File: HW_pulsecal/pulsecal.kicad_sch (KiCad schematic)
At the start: 39 parts, among them J1 BNC_CONN, J4 Conn_01x04, Q3 FDG6301N, U1 TLV9061IDBVR, U2 TLV9061IDBVR, U5 STM32G030C8Tx

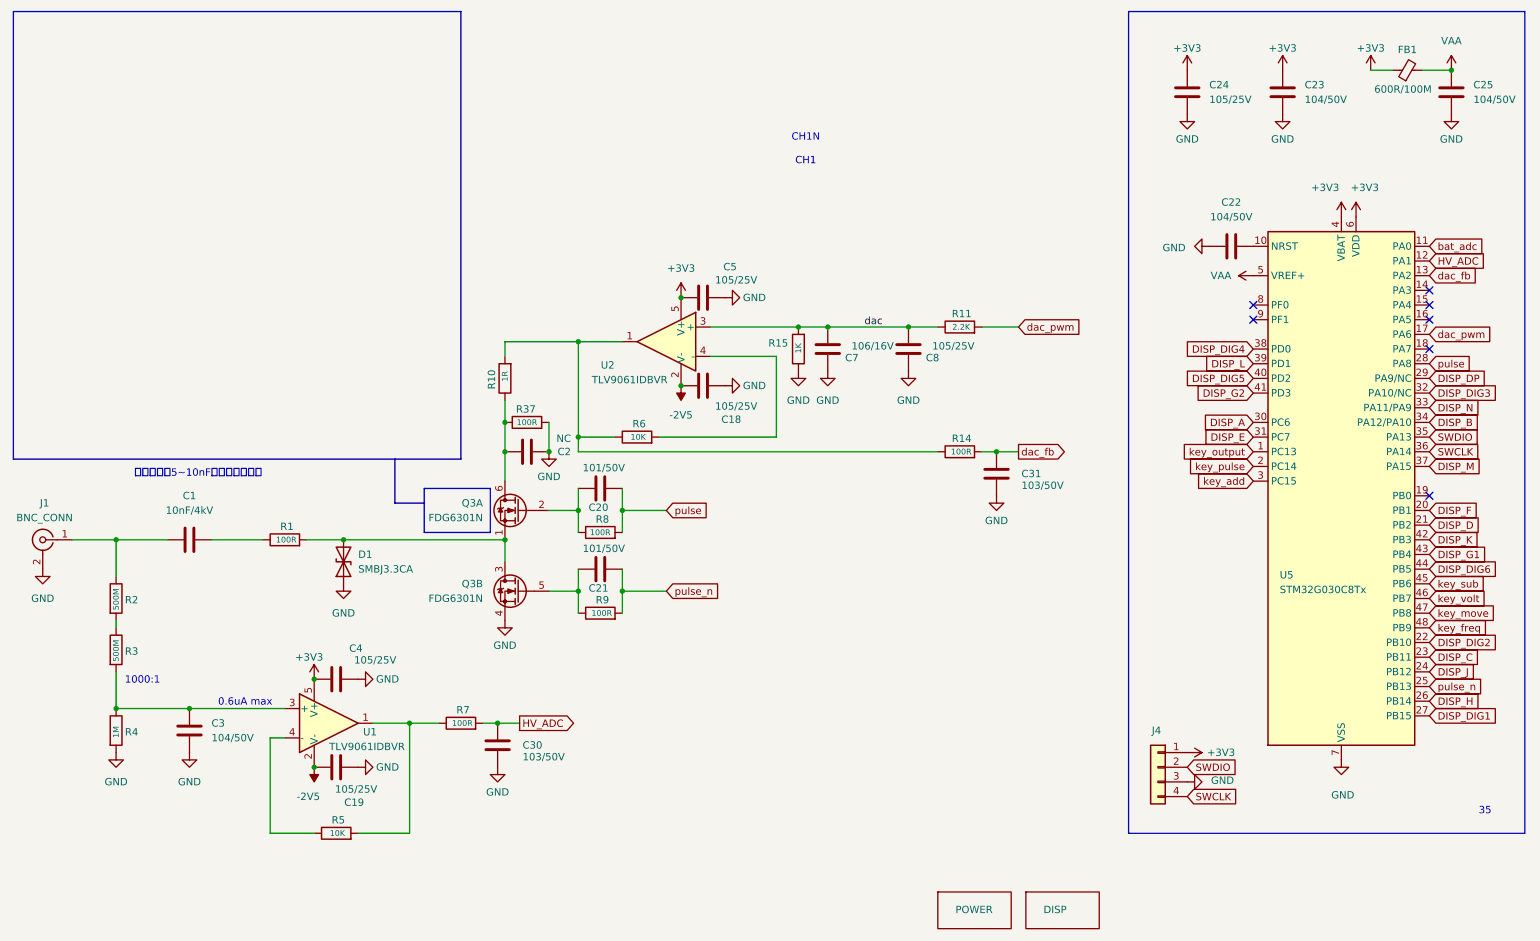
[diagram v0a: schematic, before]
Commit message: UPDATE
改连接器和输入电路
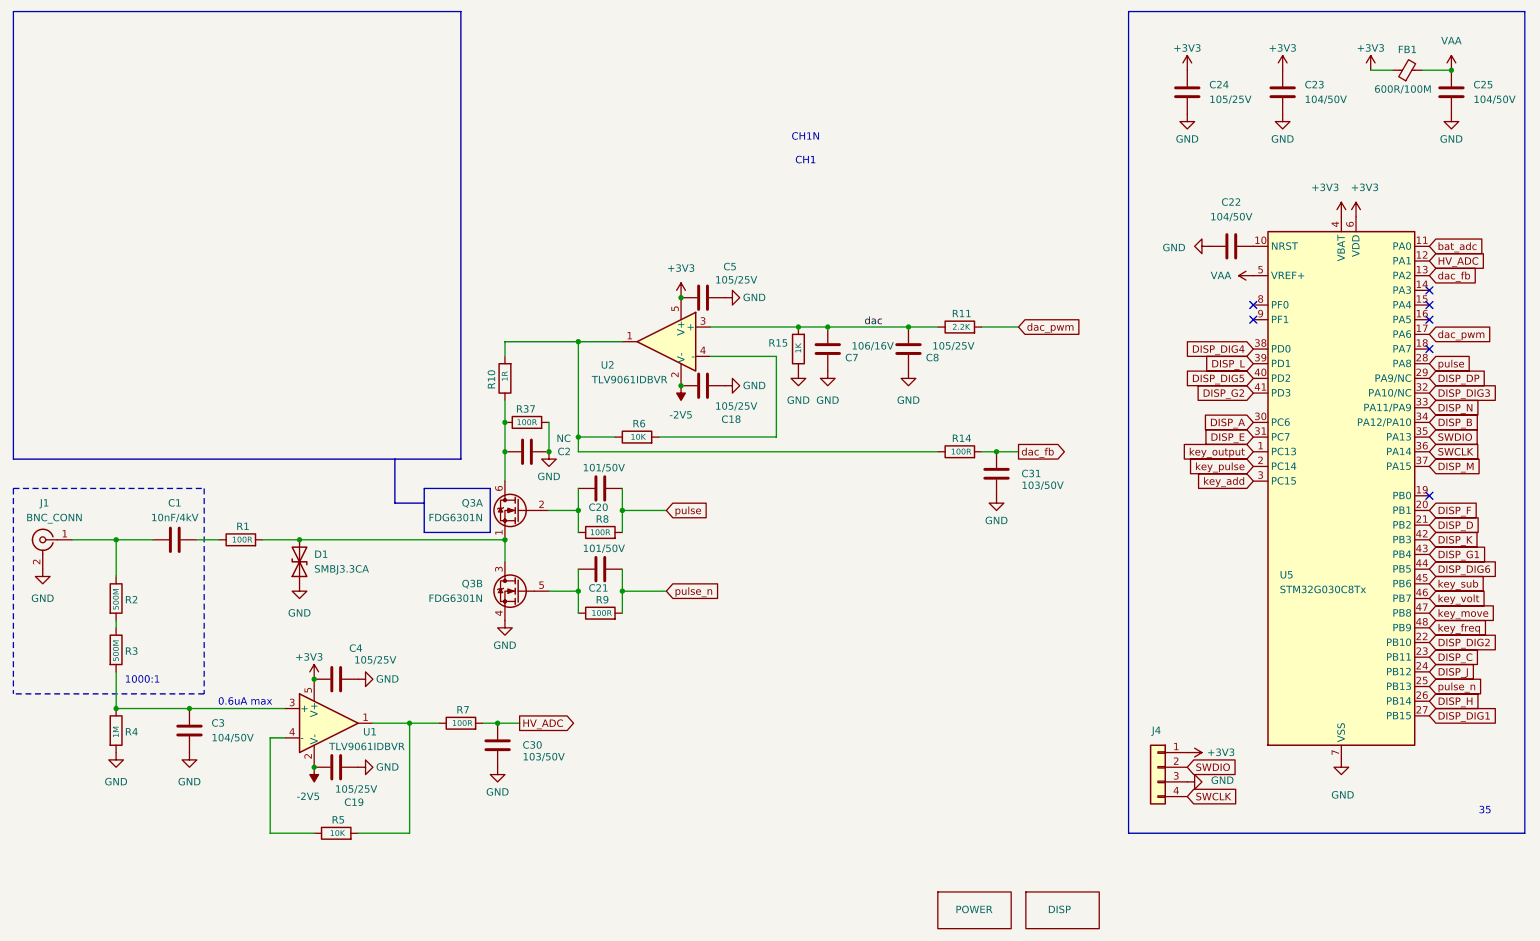
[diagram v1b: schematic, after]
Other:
- note removed: "建议用一颗5~10nF的高压电容代替"
- moved on the sheet: C1, D1, R1
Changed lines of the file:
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@@
 		)
 	)
-	(text "建议用一颗5~10nF的高压电容代替"
-		(exclude_from_sim no)
-		(at 52.324 96.52 0)
-		(effects
-			(font
-				(size 1.27 1.27)
-			)
-		)
-	)
 	(text "CH1N\n\nCH1"
 		(exclude_from_sim no)
@@
 	)
 	(junction
+		(at 69.85 107.95)
+		(diameter 0)
+		(color 0 0 0 0)
+	)
+	(junction
 		(at 118.11 116.84)
 		(diameter 0)
@@
 	)
 	(junction
-		(at 77.47 107.95)
-		(diameter 0)
-		(color 0 0 0 0)
-	)
-	(junction
 		(at 50.8 137.16)
 		(diameter 0)
@@
 	(wire
 		(pts
-			(xy 38.1 107.95) (xy 46.99 107.95)
+			(xy 38.1 107.95) (xy 44.45 107.95)
 		)
 		(stroke
@@
 	(wire
 		(pts
-			(xy 71.12 107.95) (xy 77.47 107.95)
+			(xy 63.5 107.95) (xy 69.85 107.95)
 		)
 		(stroke
@@
 	(wire
 		(pts
+			(xy 69.85 107.95) (xy 105.41 107.95)
+		)
+		(stroke
+			(width 0)
+			(type default)
+		)
+	)
+	(wire
+		(pts
 			(xy 88.9 158.75) (xy 88.9 139.7)
 		)
@@
 		)
 	)
+	(polyline
+		(pts
+			(xy 53.34 99.06) (xy 53.34 134.62)
+		)
+		(stroke
+			(width 0)
+			(type dot)
+		)
+	)
 	(wire
 		(pts
@@
 		)
 	)
+	(polyline
+		(pts
+			(xy 53.34 134.62) (xy 20.32 134.62)
+		)
+		(stroke
+			(width 0)
+			(type dot)
+		)
+	)
 	(wire
 		(pts
@@
 		)
 	)
+	(polyline
+		(pts
+			(xy 20.32 99.06) (xy 20.32 134.62)
+		)
+		(stroke
+			(width 0)
+			(type dot)
+		)
+	)
 	(wire
 		(pts
@@
 	(wire
 		(pts
-			(xy 54.61 107.95) (xy 63.5 107.95)
+			(xy 52.07 107.95) (xy 55.88 107.95)
 		)
 		(stroke
@@
 	(polyline
 		(pts
-			(xy 86.36 101.6) (xy 91.44 101.6)
+			(xy 20.32 99.06) (xy 53.34 99.06)
 		)
 		(stroke
 			(width 0)
-			(type default)
+			(type dot)
 		)
 	)
-	(wire
+	(polyline
 		(pts
-			(xy 64.77 158.75) (xy 72.39 158.75)
+			(xy 86.36 101.6) (xy 91.44 101.6)
 		)
 		(stroke
@@
 	(wire
 		(pts
-			(xy 113.03 102.87) (xy 118.11 102.87)
+			(xy 64.77 158.75) (xy 72.39 158.75)
 		)
 		(stroke
@@
 	(wire
 		(pts
-			(xy 50.8 137.16) (xy 67.31 137.16)
+			(xy 113.03 102.87) (xy 118.11 102.87)
 		)
 		(stroke
@@
 	(wire
 		(pts
-			(xy 38.1 121.92) (xy 38.1 123.19)
+			(xy 50.8 137.16) (xy 67.31 137.16)
 		)
 		(stroke
@@
 	(wire
 		(pts
-			(xy 77.47 107.95) (xy 105.41 107.95)
+			(xy 38.1 121.92) (xy 38.1 123.19)
 		)
 		(stroke
@@
 		(on_board yes)
 		(dnp no)
-		(fields_autoplaced yes)
 		(property "Reference" "J1"
 			(at 25.7174 101.6 0)
@@
 		)
 		(property "Value" "BNC_CONN"
-			(at 25.7174 104.14 0)
+			(at 27.432 104.14 0)
 			(effects
 				(font
@@
 	(symbol
 		(lib_id "Device:R")
-		(at 67.31 107.95 90)
+		(at 59.69 107.95 90)
 		(unit 1)
 		(exclude_from_sim no)
@@
 		(dnp no)
 		(property "Reference" "R1"
-			(at 68.834 105.664 90)
+			(at 61.214 105.664 90)
 			(effects
 				(font
@@
 		)
 		(property "Value" "100R"
-			(at 69.342 107.95 90)
+			(at 61.722 107.95 90)
 			(effects
 				(font
@@
 		)
 		(property "Footprint" "Resistor_THT:R_Axial_DIN0411_L9.9mm_D3.6mm_P15.24mm_Horizontal"
-			(at 67.31 109.728 90)
+			(at 59.69 109.728 90)
 			(effects
 				(font
@@
 		)
 		(property "Datasheet" "~"
-			(at 67.31 107.95 0)
+			(at 59.69 107.95 0)
 			(effects
 				(font
@@
 		)
 		(property "Description" "Resistor"
-			(at 67.31 107.95 0)
+			(at 59.69 107.95 0)
 			(effects
 				(font
@@
 	(symbol
 		(lib_id "Device:C")
-		(at 50.8 107.95 90)
+		(at 48.26 107.95 90)
 		(unit 1)
 		(exclude_from_sim no)
@@
 		(on_board yes)
 		(dnp no)
-		(fields_autoplaced yes)
 		(property "Reference" "C1"
-			(at 50.8 100.33 90)
+			(at 48.26 101.6 90)
 			(effects
 				(font
@@
 		)
 		(property "Value" "10nF/4kV"
-			(at 50.8 102.87 90)
+			(at 48.26 104.14 90)
 			(effects
 				(font
@@
 		)
 		(property "Footprint" "Capacitor_THT:C_Rect_L13.5mm_W4.0mm_P10.00mm_FKS3_FKP3_MKS4"
-			(at 54.61 106.9848 0)
+			(at 52.07 106.9848 0)
 			(effects
 				(font
@@
 		)
 		(property "Datasheet" "~"
-			(at 50.8 107.95 0)
+			(at 48.26 107.95 0)
 			(effects
 				(font
@@
 		)
 		(property "Description" "Unpolarized capacitor"
-			(at 50.8 107.95 0)
+			(at 48.26 107.95 0)
 			(effects
 				(font
@@
 	(symbol
 		(lib_id "Device:D_TVS")
-		(at 77.47 111.76 90)
+		(at 69.85 111.76 90)
 		(unit 1)
 		(exclude_from_sim no)
@@
 		(fields_autoplaced yes)
 		(property "Reference" "D1"
-			(at 80.01 110.4899 90)
+			(at 72.39 110.4899 90)
 			(effects
 				(font
@@
 		)
 		(property "Value" "SMBJ3.3CA"
-			(at 80.01 113.0299 90)
+			(at 72.39 113.0299 90)
 			(effects
 				(font
@@
 		)
 		(property "Footprint" "Diode_SMD:D_SMB"
-			(at 77.47 111.76 0)
+			(at 69.85 111.76 0)
 			(effects
 				(font
@@
 		)
 		(property "Datasheet" "~"
-			(at 77.47 111.76 0)
+			(at 69.85 111.76 0)
 			(effects
 				(font
@@
 		)
 		(property "Description" "Bidirectional transient-voltage-suppression diode"
-			(at 77.47 111.76 0)
+			(at 69.85 111.76 0)
 			(effects
 				(font
@@
 	(symbol
 		(lib_id "power:GND")
-		(at 77.47 115.57 0)
+		(at 69.85 115.57 0)
 		(unit 1)
 		(exclude_from_sim no)
@@
 		(fields_autoplaced yes)
 		(property "Reference" "#PWR07"
-			(at 77.47 121.92 0)
+			(at 69.85 121.92 0)
 			(effects
 				(font
@@
 		)
 		(property "Value" "GND"
-			(at 77.47 120.65 0)
+			(at 69.85 120.65 0)
 			(effects
 				(font
@@
 		)
 		(property "Footprint" ""
-			(at 77.47 115.57 0)
+			(at 69.85 115.57 0)
 			(effects
 				(font
@@
 		)
 		(property "Datasheet" ""
-			(at 77.47 115.57 0)
+			(at 69.85 115.57 0)
 			(effects
 				(font
@@
 		)
 		(property "Description" "Power symbol creates a global label with name \"GND\" , ground"
-			(at 77.47 115.57 0)
+			(at 69.85 115.57 0)
 			(effects
 				(font
@@
 		)
 		(property "Sheetname" "DISP"
-			(at 198.628 172.72 0)
+			(at 199.39 172.72 0)
 			(effects
 				(font

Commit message: update
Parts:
- added D4: BSD3A031LV45, Diode_SMD:D_SOD-323_HandSoldering, symbol Device:D_Zener
- D1: value SMBJ3.3CA -> BSD3A031LV45; footprint Diode_SMD:D_SMB -> Diode_SMD:D_SOD-323_HandSoldering; symbol Device:D_TVS -> Device:D_Zener
- R11: value 2.2K -> 22K
- R15: value 1K -> 10K
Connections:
- net GND: now also D1.2 (A), D4.2 (A); no longer D1.1 (A1)
- net at Q3.1 (S), Q3.3 (D), R1.2: now also D1.1 (K), D4.1 (K); no longer D1.2 (A2)
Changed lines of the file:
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@@
 			)
 		)
-		(property "Value" "1K"
+		(property "Value" "10K"
 			(at 156.21 73.914 90)
 			(effects
@@
 	)
 	(symbol
+		(lib_id "Device:D_Zener")
+		(at 69.85 104.14 90)
+		(unit 1)
+		(exclude_from_sim no)
+		(in_bom yes)
+		(on_board yes)
+		(dnp no)
+		(property "Reference" "D4"
+			(at 72.39 102.8699 90)
+			(effects
+				(font
+					(size 1.27 1.27)
+				)
+				(justify right)
+			)
+		)
+		(property "Value" "BSD3A031LV45"
+			(at 72.39 105.4099 90)
+			(effects
+				(font
+					(size 1.27 1.27)
+				)
+				(justify right)
+			)
+		)
+		(property "Footprint" "Diode_SMD:D_SOD-323_HandSoldering"
+			(at 69.85 104.14 0)
+			(effects
+				(font
+					(size 1.27 1.27)
+				)
+				(hide yes)
+			)
+		)
+		(property "Datasheet" "~"
+			(at 69.85 104.14 0)
+			(effects
+				(font
+					(size 1.27 1.27)
+				)
+				(hide yes)
+			)
+		)
+		(property "Description" "Zener diode"
+			(at 69.85 104.14 0)
+			(effects
+				(font
+					(size 1.27 1.27)
+				)
+				(hide yes)
+			)
+		)
+		(pin "1"
+		)
+		(pin "2"
+		)
+		(instances
+			(project "pulsecal"
+				(path "/43467254-5f0e-4dea-8ff8-85167d0157c0"
+					(reference "D4")
+					(unit 1)
+				)
+			)
+		)
+	)
+	(symbol
 		(lib_id "Device:C")
 		(at 175.26 74.93 180)
@@
 		(on_board yes)
 		(dnp no)
-		(fields_autoplaced yes)
 		(property "Reference" "Q3"
 			(at 101.6 115.5699 0)
@@
 		)
 		(property "Value" "FDG6301N"
-			(at 101.6 118.1099 0)
+			(at 101.854 118.11 0)
 			(effects
 				(font
@@
 	)
 	(symbol
-		(lib_id "Device:D_TVS")
+		(lib_id "Device:D_Zener")
 		(at 69.85 111.76 90)
+		(mirror x)
 		(unit 1)
 		(exclude_from_sim no)
@@
 		(on_board yes)
 		(dnp no)
-		(fields_autoplaced yes)
 		(property "Reference" "D1"
-			(at 72.39 110.4899 90)
+			(at 72.39 113.0301 90)
 			(effects
 				(font
@@
 			)
 		)
-		(property "Value" "SMBJ3.3CA"
-			(at 72.39 113.0299 90)
+		(property "Value" "BSD3A031LV45"
+			(at 72.39 110.4901 90)
 			(effects
 				(font
@@
 			)
 		)
-		(property "Footprint" "Diode_SMD:D_SMB"
+		(property "Footprint" "Diode_SMD:D_SOD-323_HandSoldering"
 			(at 69.85 111.76 0)
 			(effects
@@
 			)
 		)
-		(property "Description" "Bidirectional transient-voltage-suppression diode"
+		(property "Description" "Zener diode"
 			(at 69.85 111.76 0)
 			(effects
@@
 	)
 	(symbol
+		(lib_id "power:GND")
+		(at 69.85 100.33 0)
+		(mirror x)
+		(unit 1)
+		(exclude_from_sim no)
+		(in_bom yes)
+		(on_board yes)
+		(dnp no)
+		(fields_autoplaced yes)
+		(property "Reference" "#PWR074"
+			(at 69.85 93.98 0)
+			(effects
+				(font
+					(size 1.27 1.27)
+				)
+				(hide yes)
+			)
+		)
+		(property "Value" "GND"
+			(at 69.85 95.25 0)
+			(effects
+				(font
+					(size 1.27 1.27)
+				)
+				(hide yes)
+			)
+		)
+		(property "Footprint" ""
+			(at 69.85 100.33 0)
+			(effects
+				(font
+					(size 1.27 1.27)
+				)
+				(hide yes)
+			)
+		)
+		(property "Datasheet" ""
+			(at 69.85 100.33 0)
+			(effects
+				(font
+					(size 1.27 1.27)
+				)
+				(hide yes)
+			)
+		)
+		(property "Description" "Power symbol creates a global label with name \"GND\" , ground"
+			(at 69.85 100.33 0)
+			(effects
+				(font
+					(size 1.27 1.27)
+				)
+				(hide yes)
+			)
+		)
+		(pin "1"
+		)
+		(instances
+			(project "pulsecal"
+				(path "/43467254-5f0e-4dea-8ff8-85167d0157c0"
+					(reference "#PWR074")
+					(unit 1)
+				)
+			)
+		)
+	)
+	(symbol
 		(lib_id "Amplifier_Operational:TLV9061xDBV")
 		(at 74.93 139.7 0)
@@
 			)
 		)
-		(property "Value" "2.2K"
-			(at 185.928 71.12 90)
+		(property "Value" "22K"
+			(at 185.674 71.12 90)
 			(effects
 				(font

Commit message: update
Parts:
- removed D4: BSD3A031LV45, Diode_SMD:D_SOD-323_HandSoldering, symbol Device:D_Zener
- added R12: 1R, Resistor_SMD:R_0402_1005Metric, symbol Device:R
- C2: value NC -> 105/25V
- D1: value BSD3A031LV45 -> SMBJ3.3A; footprint Diode_SMD:D_SOD-323_HandSoldering -> Diode_SMD:D_SMB
- J1: value BNC_CONN -> MHV-KE
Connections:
- net GND: now also R12.1; no longer Q3.4 (S)
- new net: Q3.4 (S), R12.2
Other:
- moved on the sheet: R6
